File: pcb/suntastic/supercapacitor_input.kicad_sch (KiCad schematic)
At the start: 9 parts, among them J3 Supercap IN

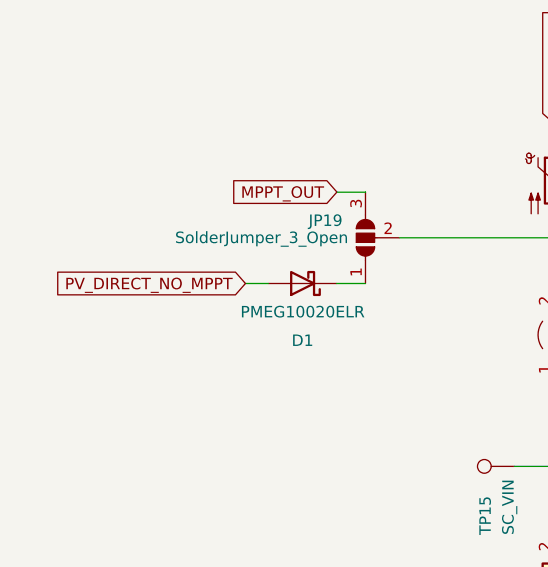
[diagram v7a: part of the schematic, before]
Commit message: Add screw terminals for external MPPT module and PV input
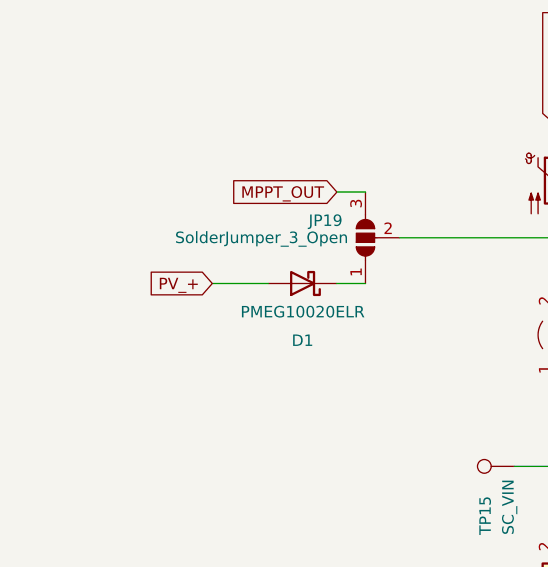
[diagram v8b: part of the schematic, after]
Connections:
- net PV_DIRECT_NO_MPPT renamed PV_+
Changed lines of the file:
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@@
     (stroke (width 0) (type default))
   )
-  (wire (pts (xy 116.205 63.5) (xy 118.745 63.5))
+  (wire (pts (xy 112.522 63.5) (xy 118.745 63.5))
     (stroke (width 0) (type default))
   )
@@
     (effects (font (size 1.27 1.27)) (justify left bottom))
   )
-  (global_label "PV_DIRECT_NO_MPPT" (shape input) (at 116.205 63.5 180) (fields_autoplaced)
+  (global_label "PV_+" (shape input) (at 112.522 63.5 180) (fields_autoplaced)
     (effects (font (size 1.27 1.27)) (justify right))
-    (property "Intersheetrefs" "${INTERSHEET_REFS}" (at 93.8864 63.5 0)
+    (property "Intersheetrefs" "${INTERSHEET_REFS}" (at 104.7176 63.5 0)
       (effects (font (size 1.27 1.27)) (justify right) hide)
     )
